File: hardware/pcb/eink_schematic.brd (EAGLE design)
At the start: 97.9 x 71.1 mm, 13 parts, among them J1 AA_BAT_PACKSMD, J2 5.5x2.1mm Barrel, Q1 FDN340P, U1 NUCLEUM, U2 LTC3531ES6-3PBF, U4 MAX6326UR29+

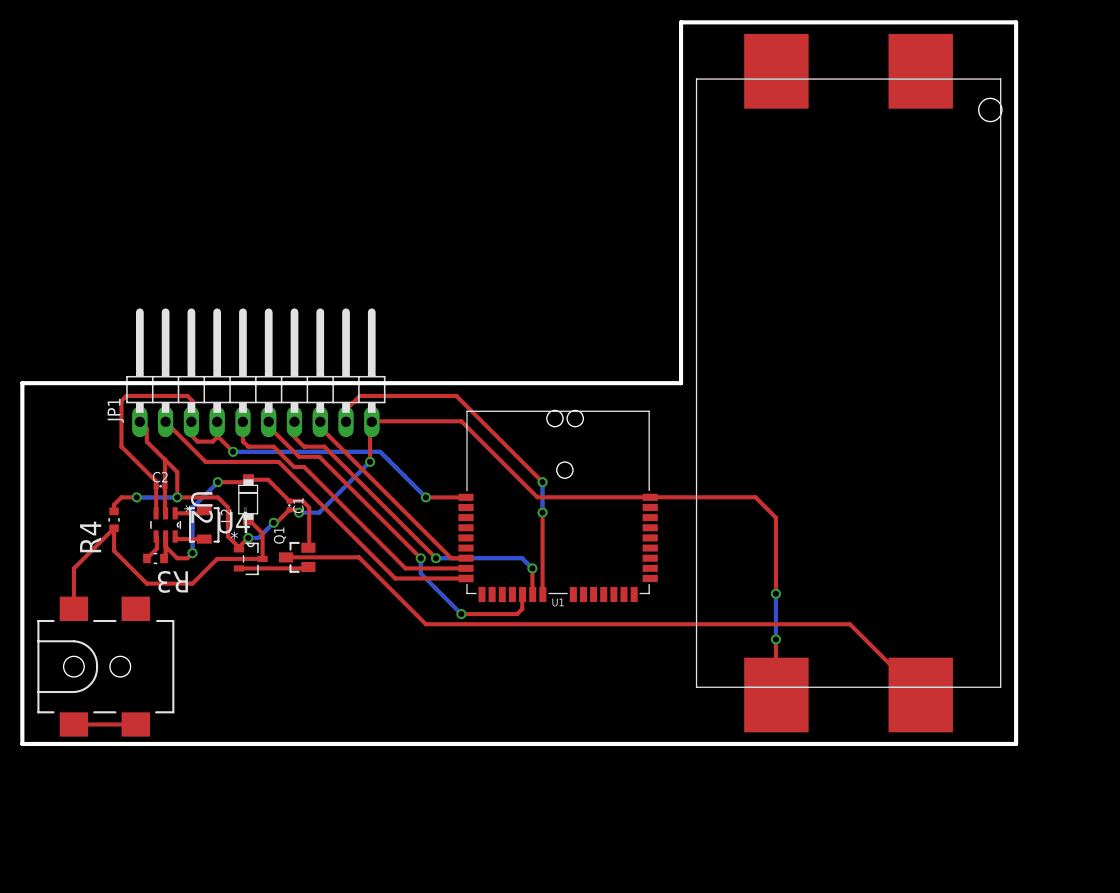
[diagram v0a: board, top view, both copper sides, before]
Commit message: centered board on origin and added measurements
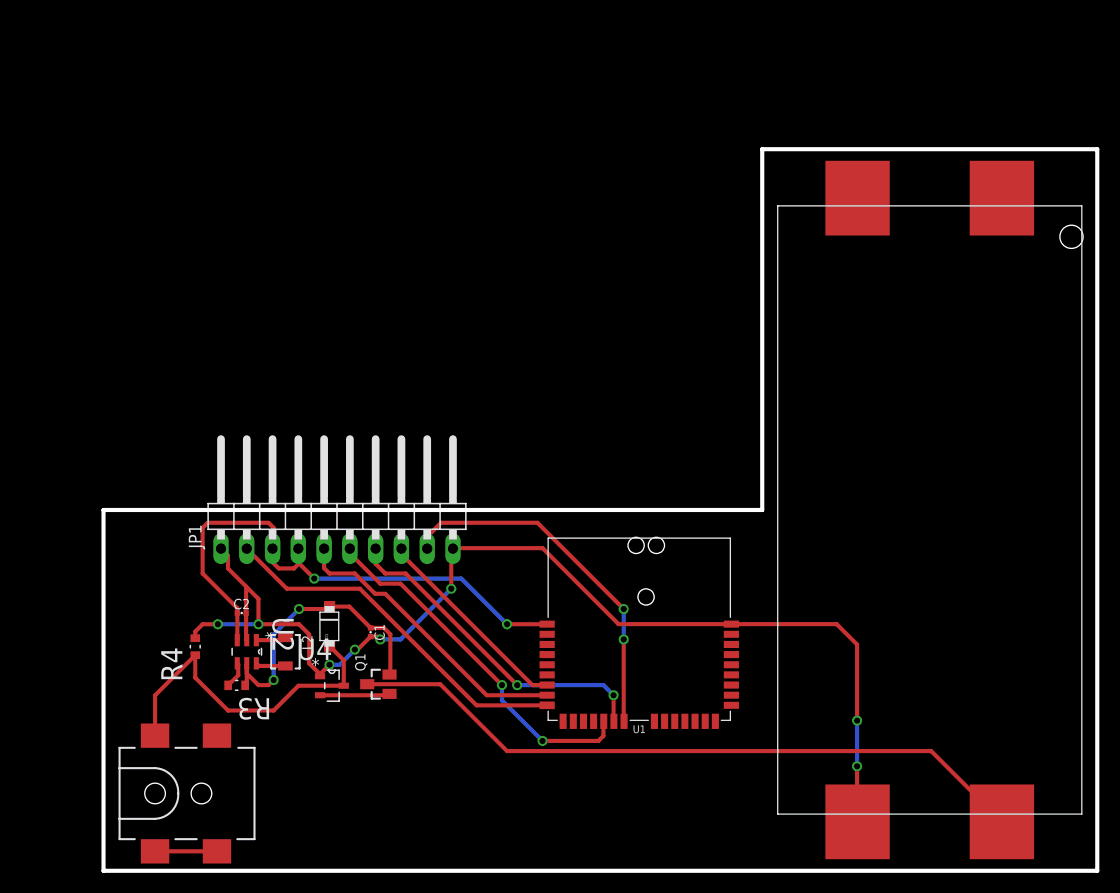
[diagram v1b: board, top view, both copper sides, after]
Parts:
- moved C1 14.8 mm to (26.6, 23.7)
- moved C2 14.8 mm to (13.8, 25.6)
- moved D1 14.8 mm to (22.5, 24.3)
- moved J1 14.8 mm to (81.7, 35.8)
- moved J2 14.8 mm to (5.31, 7.82)
- moved JP1 14.8 mm to (23.2, 35.8)
- moved L2 14.8 mm to (18.2, 21.8)
- moved Q1 14.8 mm to (27.3, 18.6)
- moved R3 14.8 mm to (13.3, 18.5)
- moved R4 14.8 mm to (9.27, 22.3)
- moved U1 14.8 mm to (44.1, 33.0)
- moved U2 14.8 mm to (14.3, 21.8)
- moved U4 14.8 mm to (22.7, 18.4)

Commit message: re-wired and created eagle part for through-hole battery pack
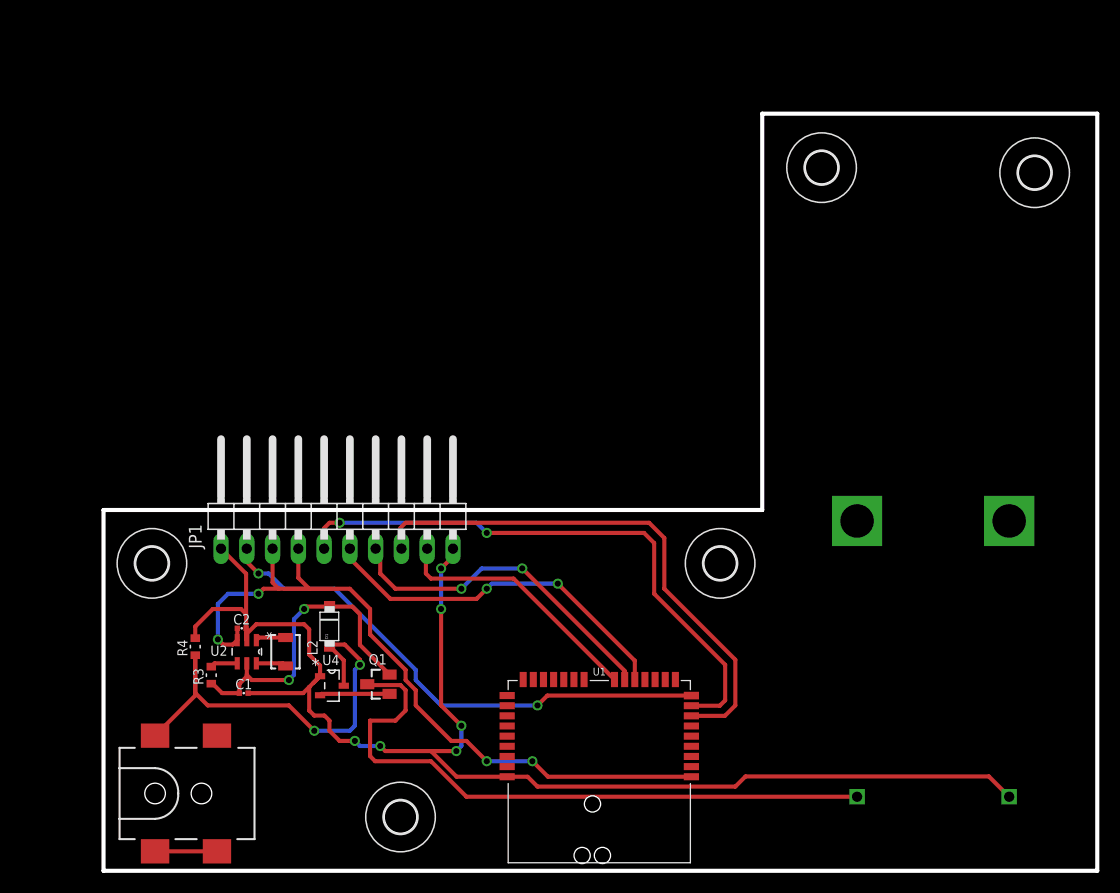
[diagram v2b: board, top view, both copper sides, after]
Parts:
- removed J1: AA_BAT_PACKSMD, connector:AA_SMD
- added BATTERY: KEYSTONEELECTRONICS2462, through_hole_battery_pack:KEYSTONEELECTRONICS2462
- added U$1, U$2, U$3, U$4, U$5: (no value), holes:3,2
- moved U1 34.9 mm to (58.1, 0.99), turned to 90 degrees
- moved C1 13.9 mm to (14.1, 17.7), turned to 0 degrees
- moved R3 2.69 mm to (10.8, 19.5), turned to 90 degrees
- moved C2 1.50 mm to (13.8, 24.1)
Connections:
- removed net N$5: J1.1+, J1.2-
- net GND: now also BATTERY.P4; no longer J1.1-
- net N$4: now also BATTERY.P3; no longer J1.2+
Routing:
- net !CS: track 20.3 -> 53.1 mm
- net TC_BUSY: track 29.1 -> 57.5 mm, vias 0 -> 2
- net GND: track 113.4 -> 138.3 mm, vias 8 -> 6
- net VCC: track 54.8 -> 73.5 mm, vias 2 -> 4
- net ENABLE: track 36.0 -> 52.0 mm, vias 0 -> 2
- net N$2: track 33.3 -> 45.6 mm, vias 0 -> 2
- net SPI_CLK: track 35.7 -> 25.4 mm, vias 2 -> 0
- net N$4: track 68.2 -> 63.1 mm
- net N$3: track 28.8 -> 31.5 mm
- net SPI_MISO: track 35.6 -> 36.3 mm
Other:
- board size 97.9 x 71.1 mm -> 97.9 x 74.6 mm

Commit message: wiring is good + added GND plane
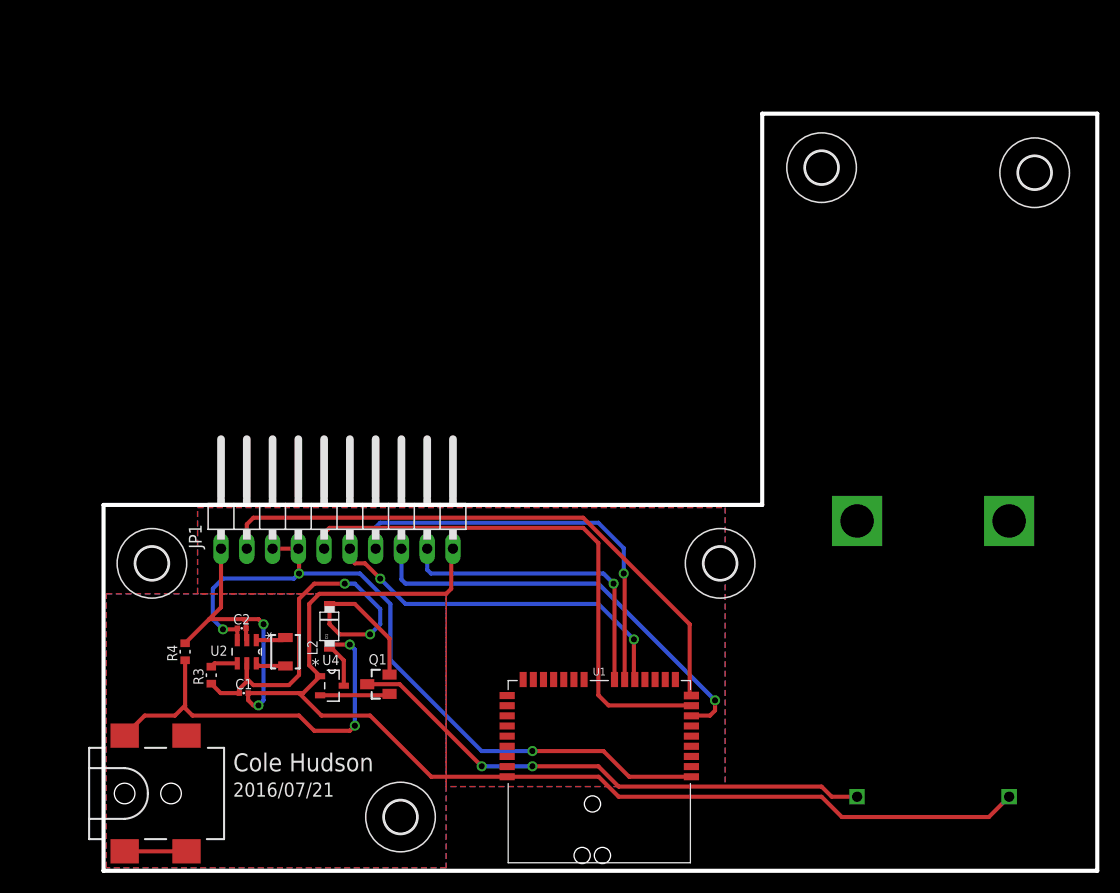
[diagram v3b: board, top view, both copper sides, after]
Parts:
- moved J2 3.00 mm to (2.31, 7.82)
- moved R4 1.12 mm to (8.27, 21.8)
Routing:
- net N$3: track 31.5 -> 50.9 mm
- net !CS: track 53.1 -> 42.4 mm, vias 0 -> 1
- net N$4: track 63.1 -> 52.9 mm, vias 0 -> 2
- net SPI_MOSI: track 33.2 -> 40.8 mm, vias 2 -> 1
- net ENABLE: track 52.0 -> 57.8 mm, vias 2 -> 0
- net SPI_CLK: track 25.4 -> 30.5 mm, vias 0 -> 1
- net TC_BUSY: track 57.5 -> 54.0 mm, vias 2 -> 0
- net VCC: track 73.5 -> 71.4 mm, vias 4 -> 3
- net N$2: track 45.6 -> 44.5 mm
- net GND: track 138.3 -> 138.6 mm, vias 6 -> 2
- added copper zone on layer 1, net GND
- added copper zone on layer 16, net GND
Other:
- outline, holes or cut-outs redrawn
- board text added: "2016/07/21"
- board text added: "Cole Hudson"
